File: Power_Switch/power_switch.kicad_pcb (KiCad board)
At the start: 2 copper layers, 13 x 18.5 mm, 3 parts, among them J1 Conn_01x02_Pin, J2 Conn_01x02_Socket, SW1 SW_SPDT

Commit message: small changes - probably wont use
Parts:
- added GND: TestPoint, TestPoint:TestPoint_Pad_D1.5mm, F.Cu at (159.3, 50.8)
- added H1: MountingHole, MountingHole:MountingHole_2.7mm_M2.5, F.Cu at (143.3, 42.7)
- added H2: MountingHole, MountingHole:MountingHole_2.7mm_M2.5, F.Cu at (160.3, 42.4)
- added H3: MountingHole, MountingHole:MountingHole_2.7mm_M2.5, F.Cu at (154.9, 55.1)
- added V_BAT: TestPoint, TestPoint:TestPoint_Pad_D1.5mm, F.Cu at (159.3, 47.0)
- J1, J2: footprint Connector_JST:JST_SH_BM02B-SRSS-TB_1x02-1MP_P1.00mm_Vertical -> Connector_JST:JST_SH_SM02B-SRSS-TB_1x02-1MP_P1.00mm_Horizontal
- moved J1 11.8 mm to (161.3, 55.1), turned to 90 degrees
- moved J2 7.17 mm to (148.8, 55.1), turned to 0 degrees
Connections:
- net Net-(J1-Pin_1) renamed /V_BAT
- net Net-(J1-Pin_2) renamed GND
- J2 pad 1: Net-(J2-Pin_1) -> /V_BAT_SWITCHED
- SW1 pad 1: unconnected-(SW1-A-Pad1) -> /V_BAT_SWITCHED
- SW1 pad 3: Net-(J2-Pin_1) -> unconnected-(SW1-C-Pad3)
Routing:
- net /V_BAT: track 4.75 -> 19.1 mm
- net GND: track 7.77 -> 0.00 mm
- net Net-(J2-Pin_1): track 4.59 -> 0.00 mm
- net /V_BAT_SWITCHED: track 0.00 -> 3.21 mm
- added copper zone on B.Cu, net GND
- added copper zone on F.Cu, net GND
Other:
- board size 13 x 18.5 mm -> 24.1 x 19.1 mm

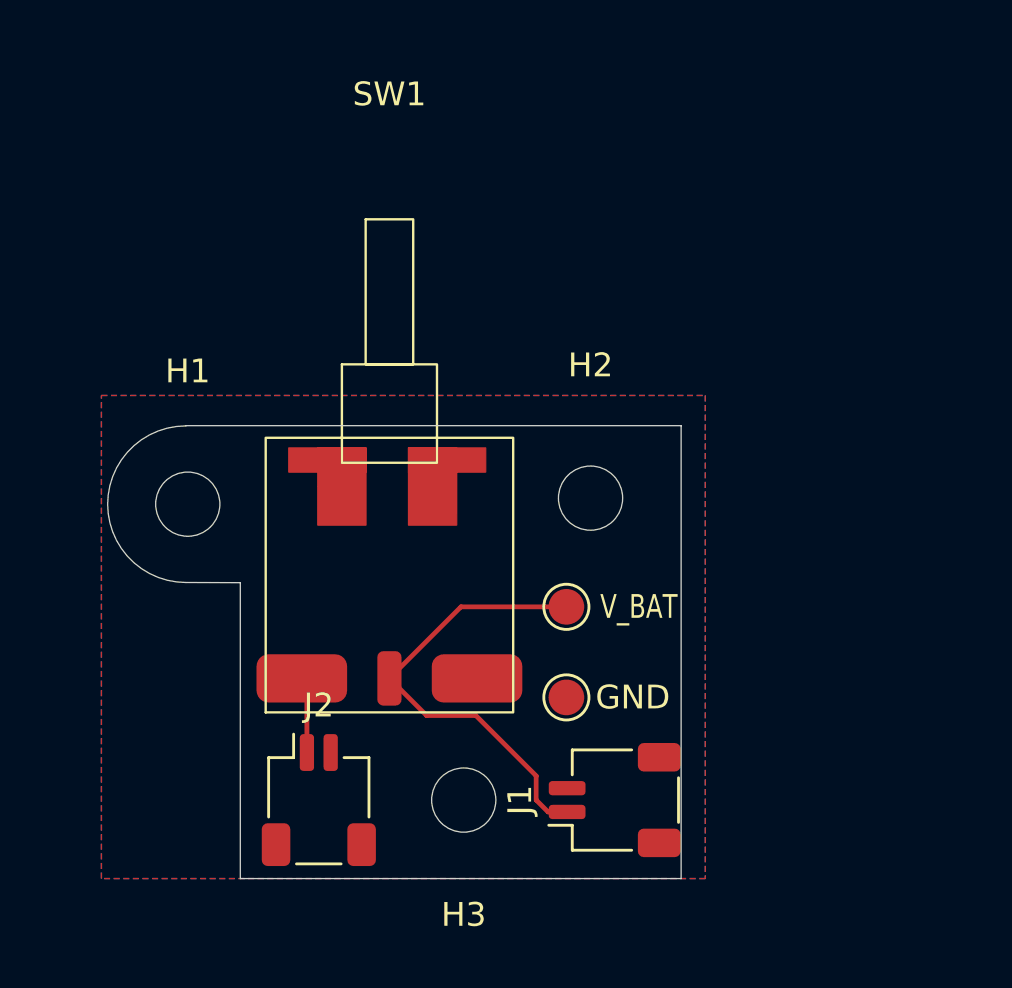
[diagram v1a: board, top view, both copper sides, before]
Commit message: Switch_LED_daughter_board done
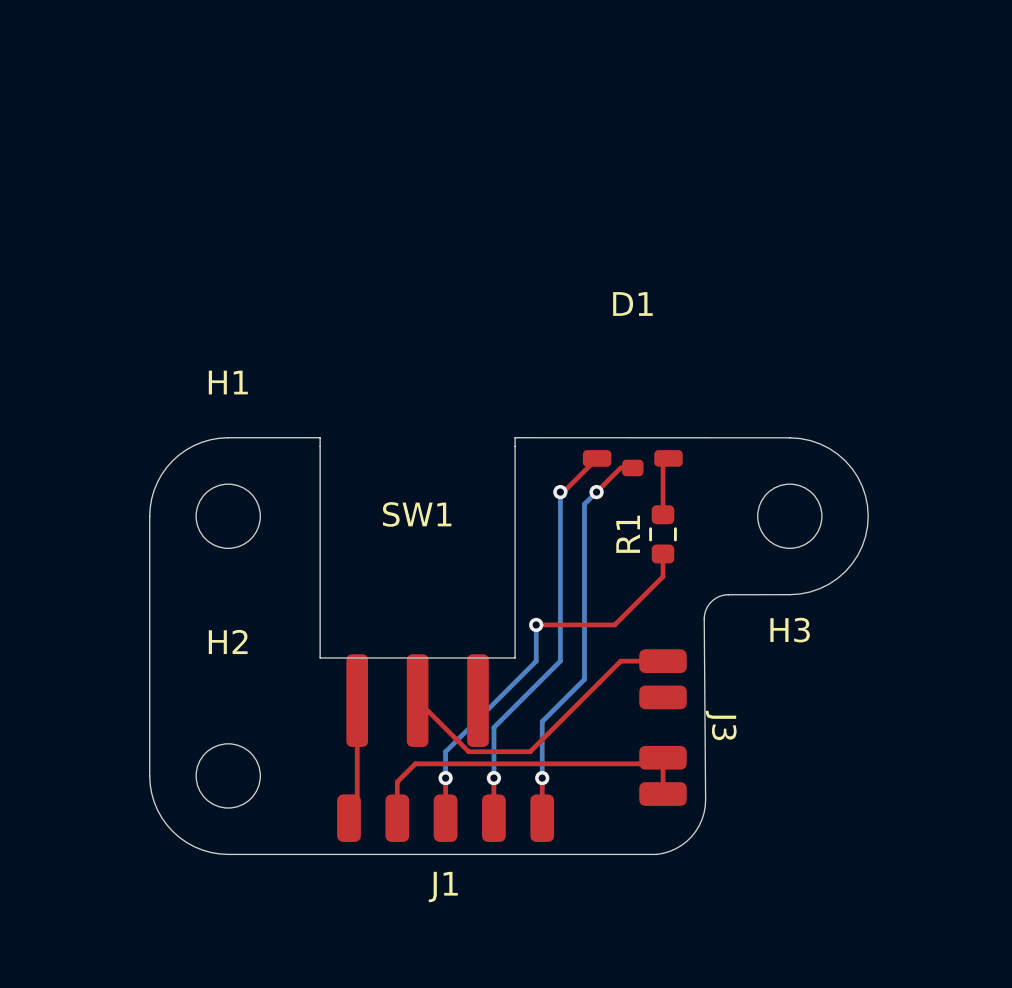
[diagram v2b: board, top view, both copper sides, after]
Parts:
- removed GND, V_BAT: TestPoint, TestPoint:TestPoint_Pad_D1.5mm
- removed J2: Conn_01x02_Socket, Connector_JST:JST_SH_SM02B-SRSS-TB_1x02-1MP_P1.00mm_Horizontal
- added D1: LED_Dual_KAK, JohnDeereLibrary:LED_Wurth_WL-SBSW, F.Cu at (162.1, 41.1)
- added J3: Conn_01x04_Socket, JohnDeereLibrary:4_pad_connector, F.Cu at (163.3, 52.1)
- added R1: 200R, Resistor_SMD:R_0603_1608Metric, F.Cu at (163.3, 43.9)
- J1: value Conn_01x02_Pin -> Conn_01x05_Socket; footprint Connector_JST:JST_SH_SM02B-SRSS-TB_1x02-1MP_P1.00mm_Horizontal -> JohnDeereLibrary:5_pad_connector
- SW1: footprint JohnDeereLibrary:ET01M3D1SAPE -> JohnDeereLibrary:ET01MD1CBE
- moved H2 19.2 mm to (145.0, 54.1)
- moved H3 18.2 mm to (168.7, 43.2)
- moved SW1 7.31 mm to (153.0, 48.1)
- moved J1 7.15 mm to (154.2, 55.9), turned to 0 degrees
- moved H1 1.78 mm to (145.0, 43.2)
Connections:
- J1 pad 1: /V_BAT -> /V_BAT_SWITCHED
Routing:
- net Net-(D1-K1): track 0.00 -> 17.0 mm, vias 0 -> 2
- net Net-(J1-Pin_3): track 0.00 -> 16.8 mm, vias 0 -> 2
- net Net-(D1-K2): track 0.00 -> 16.6 mm, vias 0 -> 2
- net GND: track 0.00 -> 14.6 mm
- net /V_BAT: track 19.1 -> 12.8 mm
- net Net-(D1-A): track 0.00 -> 2.57 mm
- net /V_BAT_SWITCHED: track 3.21 -> 5.09 mm
- removed copper zone on B.Cu, net GND
- removed copper zone on F.Cu, net GND
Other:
- board size 24.1 x 19.1 mm -> 30.2 x 17.5 mm

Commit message: small changes to UX for charging
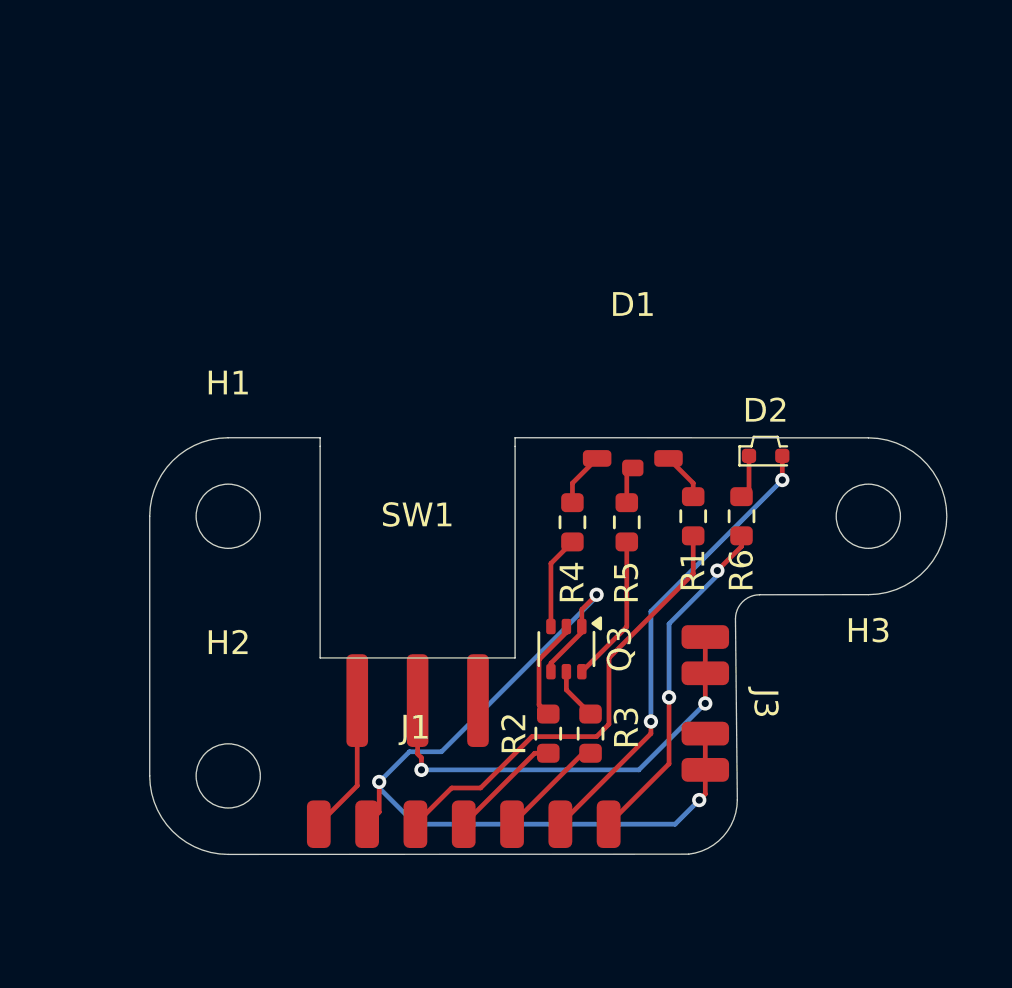
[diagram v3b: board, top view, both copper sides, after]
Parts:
- added D2: LED, JohnDeereLibrary:LED_WURTH_155060AS75300, F.Cu at (167.6, 40.6)
- added Q3: MMDT2222A, Package_TO_SOT_SMD:SOT-363_SC-70-6, F.Cu at (159.3, 48.8)
- added R2: 250R, Resistor_SMD:R_0603_1608Metric, F.Cu at (158.5, 52.3)
- added R3: 250R, Resistor_SMD:R_0603_1608Metric, F.Cu at (160.3, 52.3)
- added R4: 250R, Resistor_SMD:R_0603_1608Metric, F.Cu at (159.5, 43.4)
- added R5: 250R, Resistor_SMD:R_0603_1608Metric, F.Cu at (161.8, 43.4)
- added R6: 1k, Resistor_SMD:R_0603_1608Metric, F.Cu at (166.6, 43.2)
- J1: value Conn_01x05_Socket -> Conn_01x07_Socket; footprint JohnDeereLibrary:5_pad_connector -> JohnDeereLibrary:7_pad_connector
- R1: value 200R -> 250R
- moved H3 3.30 mm to (172.0, 43.2)
- moved J3 2.05 mm to (165.1, 51.1)
- moved R1 1.48 mm to (164.6, 43.2)
- moved J1 1.30 mm to (152.9, 56.1)
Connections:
- net /V_BAT_SWITCHED renamed VBATT_SW
- net GND renamed BATT_GND
- net Net-(J1-Pin_3) renamed LED_SPLY_V
- D1 pad 1: Net-(D1-K2) -> Net-(D1-R)
- D1 pad 3: Net-(D1-K1) -> Net-(D1-G)
- J1 pad 4: Net-(D1-K1) -> RED_CTRL
- J1 pad 5: Net-(D1-K2) -> GRN_CTRL
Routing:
- net BATT_GND: track 14.6 -> 36.1 mm, vias 0 -> 3
- net CHG_LED_V: track 0.00 -> 19.4 mm, vias 0 -> 2
- net Net-(D1-K1): track 17.0 -> 0.00 mm, vias 2 -> 0
- net Net-(D1-K2): track 16.6 -> 0.00 mm, vias 2 -> 0
- net CHR_LED_R: track 0.00 -> 14.4 mm, vias 0 -> 2
- net Net-(Q3A-C1): track 0.00 -> 6.24 mm
- net /V_BAT: track 12.8 -> 18.9 mm, vias 0 -> 2
- net RED_CTRL: track 0.00 -> 4.79 mm
- net GRN_CTRL: track 0.00 -> 4.54 mm
- net Net-(Q3A-B1): track 0.00 -> 4.32 mm
- net Net-(Q3B-C2): track 0.00 -> 3.93 mm
- net LED_SPLY_V: track 16.8 -> 19.3 mm, vias 2 -> 0
- net Net-(D1-G): track 0.00 -> 2.29 mm
- net Net-(Q3B-B2): track 0.00 -> 2.20 mm
- net Net-(D2-K): track 0.00 -> 1.85 mm
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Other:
- board size 30.2 x 17.5 mm -> 33.5 x 17.5 mm

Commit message: Finished Switch PCB - Almost done with Keyboard (Need to fix 3v3 and GND)
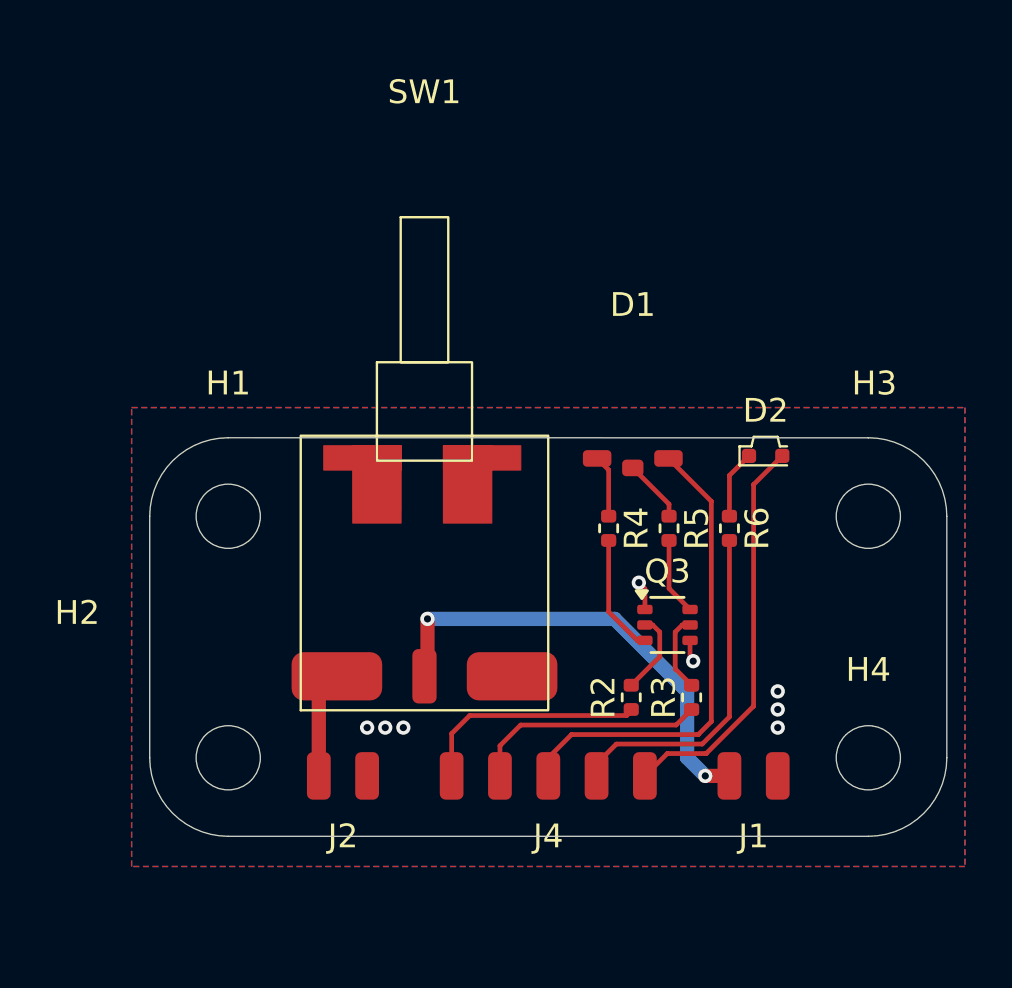
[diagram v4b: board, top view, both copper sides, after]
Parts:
- removed J3: Conn_01x04_Socket, JohnDeereLibrary:4_pad_connector
- removed R1: 250R, Resistor_SMD:R_0603_1608Metric
- added H4: MountingHole, MountingHole:MountingHole_2.7mm_M2.5, F.Cu at (172.0, 53.3)
- added J2: Conn_01x02_Pin, JohnDeereLibrary:2_pad_connector, F.Cu at (149.9, 54.1)
- added J4: Conn_01x05_Pin, JohnDeereLibrary:5_pad_connector, F.Cu at (158.5, 54.1)
- J1: value Conn_01x07_Socket -> Conn_01x02_Pin; footprint JohnDeereLibrary:7_pad_connector -> JohnDeereLibrary:2_pad_connector
- R2, R3, R4, R5, R6: footprint Resistor_SMD:R_0603_1608Metric -> Resistor_SMD:R_0402_1005Metric
- SW1: footprint JohnDeereLibrary:ET01MD1CBE -> JohnDeereLibrary:ET01M3D1SAPE
- moved J1 14.4 mm to (167.1, 54.1)
- moved SW1 7.31 mm to (153.3, 40.8)
- moved R3 4.52 mm to (164.5, 50.8)
- moved Q3 4.37 mm to (163.5, 47.8), turned to 0 degrees
- moved R2 3.81 mm to (162.0, 50.8)
- moved R5 1.80 mm to (163.6, 43.7)
- moved R4 1.55 mm to (161.0, 43.7)
- moved H2 0.76 mm to (145.0, 53.3)
- moved R6 0.72 mm to (166.1, 43.7)
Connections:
- D1 pad 2: Net-(D1-V) -> LED_SPLY_V
- J1 pad 1: VBATT_SW -> /V_BAT
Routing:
- net BATT_GND: track 36.1 -> 2.16 mm, vias 3 -> 8
- net GRN_CTRL: track 4.54 -> 9.96 mm
- net RED_CTRL: track 4.79 -> 9.79 mm
- net Net-(Q3A-C1): track 6.24 -> 3.27 mm
- net CHG_LED_V: track 19.4 -> 16.8 mm, vias 2 -> 0
- net Net-(D1-V): track 2.36 -> 0.00 mm
- net VBATT_SW: track 5.87 -> 4.51 mm
- net Net-(D1-R): track 1.57 -> 2.66 mm
- net Net-(Q3B-C2): track 3.93 -> 5.03 mm
- net Net-(Q3B-B2): track 2.20 -> 3.27 mm
- net Net-(D2-K): track 1.85 -> 2.88 mm
- net Net-(Q3A-B1): track 4.32 -> 3.48 mm
- net LED_SPLY_V: track 19.3 -> 20.1 mm
- net /V_BAT: track 18.9 -> 19.5 mm
- net CHR_LED_R: track 14.4 -> 14.3 mm, vias 2 -> 0
- added copper zone on B.Cu, net BATT_GND
- added copper zone on F.Cu, net BATT_GND
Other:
- board size 33.5 x 17.5 mm -> 33.5 x 16.8 mm

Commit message: small changes to led
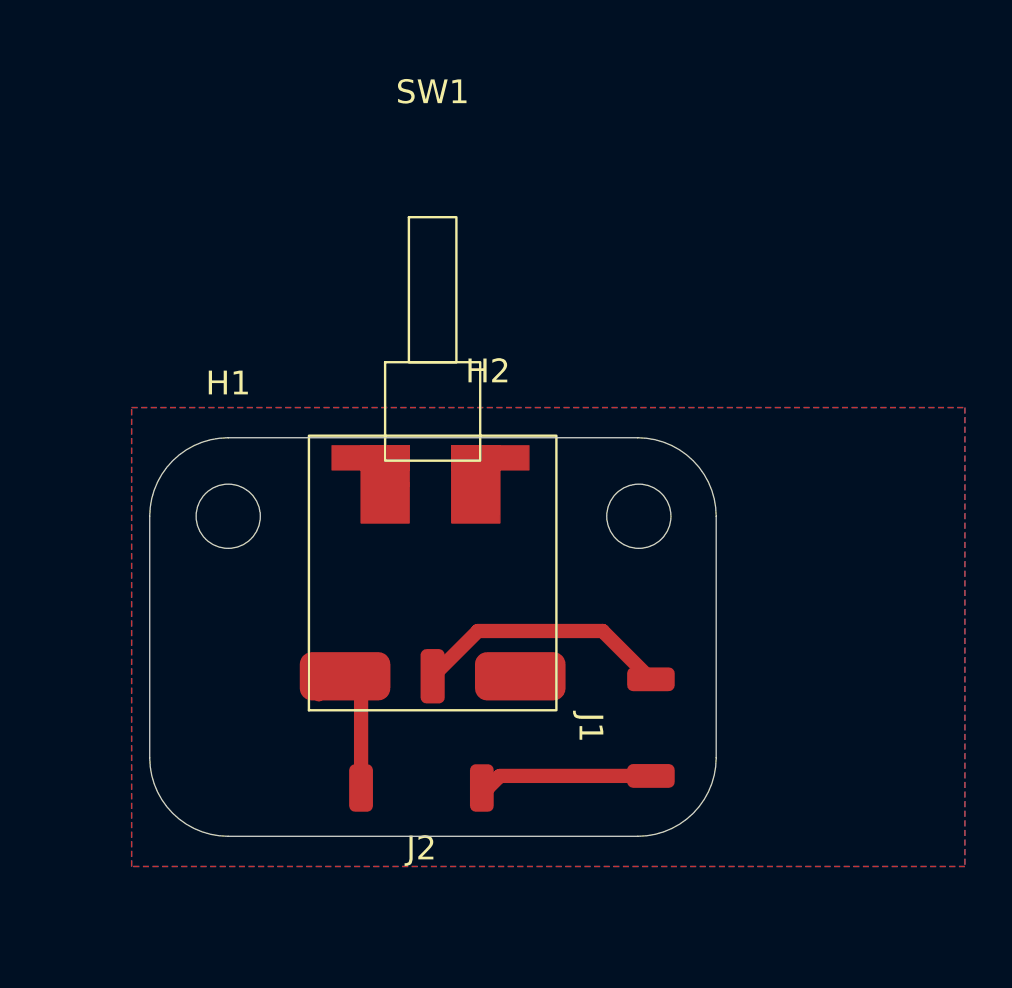
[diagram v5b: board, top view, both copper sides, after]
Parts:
- removed D1: LED_Dual_KAK, JohnDeereLibrary:LED_Wurth_WL-SBSW
- removed D2: LED, JohnDeereLibrary:LED_WURTH_155060AS75300
- removed H3, H4: MountingHole, MountingHole:MountingHole_2.7mm_M2.5
- removed J4: Conn_01x05_Pin, JohnDeereLibrary:5_pad_connector
- removed Q3: MMDT2222A, Package_TO_SOT_SMD:SOT-363_SC-70-6
- removed R2, R3, R4, R5: 250R, Resistor_SMD:R_0402_1005Metric
- removed R6: 1k, Resistor_SMD:R_0402_1005Metric
- moved H2 20.0 mm to (162.3, 43.2)
- moved J1 4.77 mm to (162.8, 52.1), turned to -90 degrees
- moved J2 3.34 mm to (153.2, 54.6)
- moved SW1 0.34 mm to (153.6, 40.8)
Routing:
- net LED_SPLY_V: track 20.1 -> 0.00 mm
- net CHG_LED_V: track 16.8 -> 0.00 mm
- net CHR_LED_R: track 14.3 -> 0.00 mm
- net GRN_CTRL: track 9.96 -> 0.00 mm
- net RED_CTRL: track 9.79 -> 0.00 mm
- net /V_BAT: track 19.5 -> 10.8 mm, vias 2 -> 0
- net BATT_GND: track 2.16 -> 7.32 mm, vias 8 -> 0
- net Net-(Q3B-C2): track 5.03 -> 0.00 mm
- net Net-(Q3A-B1): track 3.48 -> 0.00 mm
- net Net-(Q3B-B2): track 3.27 -> 0.00 mm
- net Net-(Q3A-C1): track 3.27 -> 0.00 mm
- net Net-(D2-K): track 2.88 -> 0.00 mm
- net Net-(D1-R): track 2.66 -> 0.00 mm
- net Net-(D1-G): track 2.63 -> 0.00 mm
- net VBATT_SW: track 4.51 -> 6.05 mm
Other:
- board size 33.5 x 16.8 mm -> 23.8 x 16.8 mm

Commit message: Power switch done
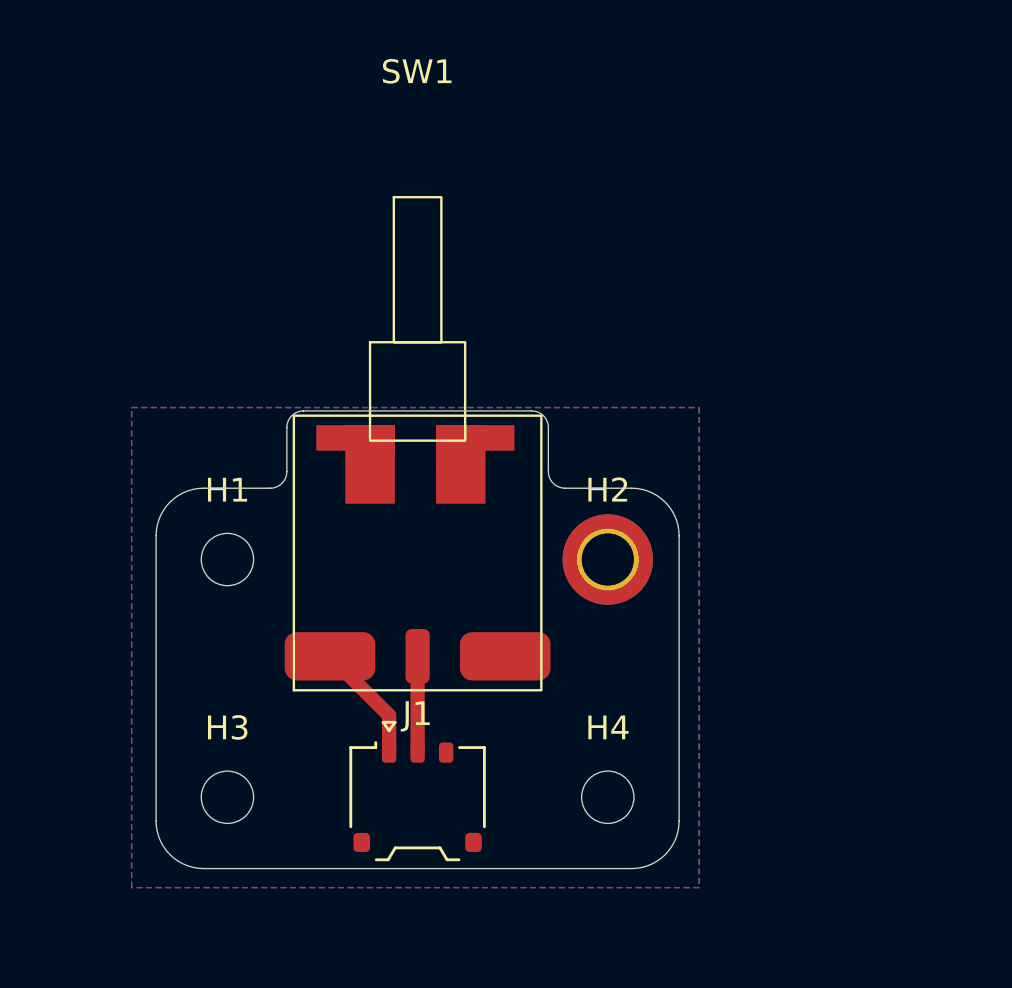
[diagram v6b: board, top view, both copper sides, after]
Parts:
- removed J2: Conn_01x02_Pin, JohnDeereLibrary:2_pad_connector
- added H3: MountingHole, MountingHole:MountingHole_2.2mm_M2_ISO14580, F.Cu at (145.0, 55.0)
- added H4: MountingHole, MountingHole:MountingHole_2.2mm_M2_ISO14580, F.Cu at (161.0, 55.0)
- H1: footprint MountingHole:MountingHole_2.7mm_M2.5 -> MountingHole:MountingHole_2.2mm_M2_ISO14580
- H2: footprint MountingHole:MountingHole_2.7mm_M2.5 -> MountingHole:MountingHole_2.2mm_M2_ISO14580_Pad_TopBottom
- J1: value Conn_01x02_Pin -> Conn_01x03_Pin; footprint JohnDeereLibrary:2_pad_connector -> Connector_Molex:Molex_Pico-EZmate_78171-0003_1x03-1MP_P1.20mm_Vertical
- moved J1 10.2 mm to (153.0, 55.0), turned to 0 degrees
- moved H2 2.24 mm to (161.0, 45.0)
- moved H1 1.82 mm to (145.0, 45.0)
- moved SW1 1.05 mm to (153.0, 40.0)
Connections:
- J1 pad 1: /V_BAT -> +BATT
- J1 pad 2: BATT_GND -> Net-(J1-Pin_2)
- SW1 pad 1: VBATT_SW -> +BATT
- SW1 pad 2: /V_BAT -> Net-(J1-Pin_2)
- SW1 pad 3: unconnected-(SW1-C-Pad3) -> GND
- SW1 pad MP: BATT_GND -> GND
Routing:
- net /V_BAT: track 10.8 -> 0.00 mm
- net BATT_GND: track 7.32 -> 0.00 mm
- net VBATT_SW: track 6.05 -> 0.00 mm
- net +BATT: track 0.00 -> 5.08 mm
- net Net-(J1-Pin_2): track 0.00 -> 4.05 mm
- added copper zone on B.Cu, net GND
- added copper zone on F.Cu, net GND
- removed copper zone on B.Cu, net BATT_GND
- removed copper zone on F.Cu, net BATT_GND
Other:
- board size 23.8 x 16.8 mm -> 22 x 19.2 mm
